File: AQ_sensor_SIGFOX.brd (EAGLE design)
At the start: 110 x 64 mm, 49 parts, among them IC2 MCP73831/OT, J1 F-1X03-SIP-100-32, SW1 PCM12SMTR, SW2 PCM12SMTR, U2 TEXAS_INSTRUMENTS_SN74HC125TE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, U3 TEXAS_INSTRUMENTS_LM1117IMP-3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, X1 53048-08, X2 SIMLOCK-C707_10M006_512_2, X4 50 Ohms

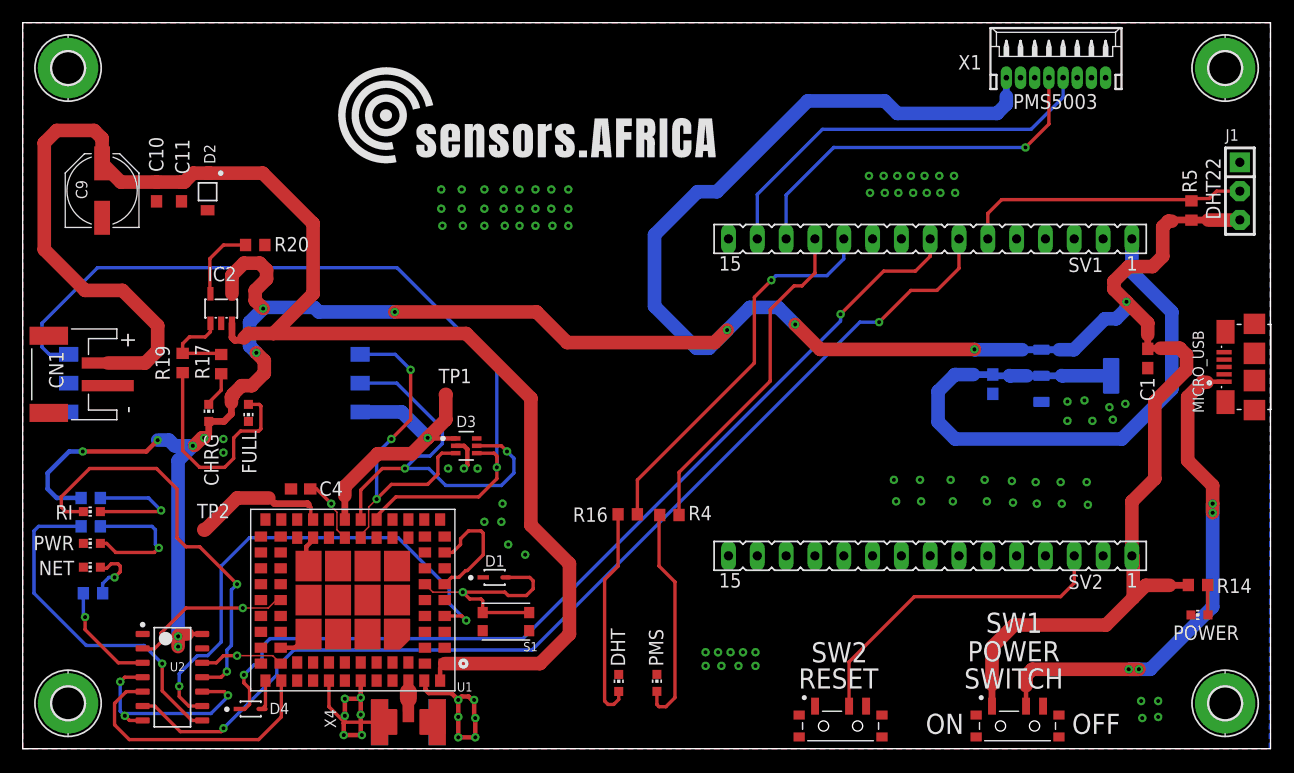
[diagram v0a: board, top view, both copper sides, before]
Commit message: Added sigfox circuit
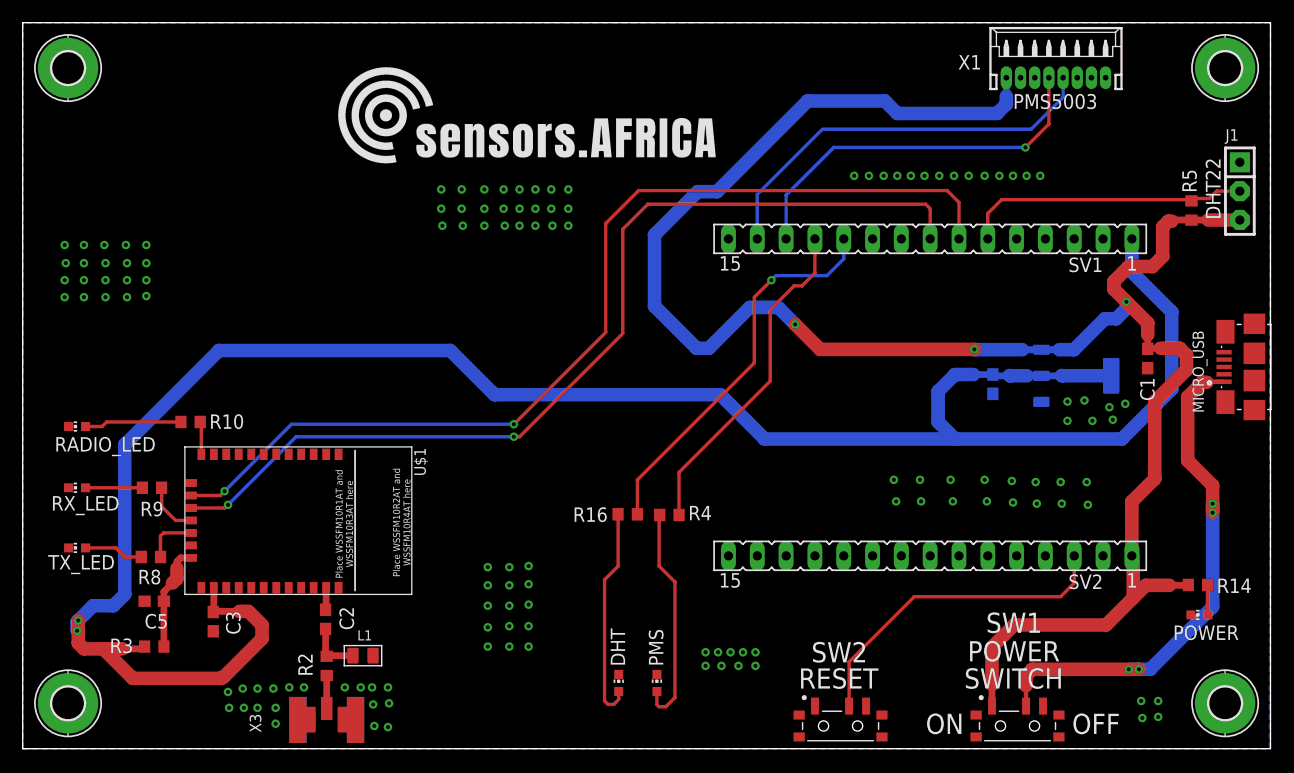
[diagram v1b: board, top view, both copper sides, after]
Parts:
- removed C10: 33pF, rcl:C0603
- removed C11: 10pF, rcl:C0603
- removed C4: 10uF, rcl:C0603
- removed C9: 100uF, rcl:PANASONIC_D
- removed CHRG, PWR: RED, led:CHIP-LED0603
- removed CN1: (no value), AQ_sensor_GSM:JST-PH-2-SMT-RA
- removed D1, D4: ON_SEMI_1N4148WSON_SEMI_1N4148WS_0_0, AQ_sensor_GSM:ON_SEMI_1N4148WS_0
- removed D2: ON_SEMICONDUCTOR_MMSZ5231BT1GON_SEMICONDUCTOR_MMSZ5231BT1G_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, AQ_sensor_GSM:ON_SEMICONDUCTOR_MMSZ5231BT1G_0
- removed D3: SEMTECH_SMF05CSEMTECH_SMF05C_0_0, AQ_sensor_GSM:SEMTECH_SMF05C_0
- removed FULL, NET: YELLOW, led:CHIP-LED0603
- removed IC2: MCP73831/OT, AQ_sensor_GSM:SOT23-5L
- removed R1, R17, R19, R6, R7: 470, rcl:R0603
- removed R20: 2K, rcl:R0603
- removed RI: ORANGE, led:CHIP-LED0603
- removed S1: KMR621NGLFS, AQ_sensor_GSM:SW_KMR621NGLFS
- removed TP1, TP2: TPB1,27, testpad:B1,27
- removed U1: (no value), AQ_sensor_GSM:SIM800L
- removed U2: TEXAS_INSTRUMENTS_SN74HC125TEXAS_INSTRUMENTS_SN74HC125_0_0, AQ_sensor_GSM:TEXAS_INSTRUMENTS_SN74HC125_0
- removed X2: SIMLOCK-C707_10M006_512_2, AQ_sensor_GSM:C707_10M006_512_2
- removed X4: 50 Ohms, AQ_sensor_GSM:SMA_EDGELAUNCH_UFL
- added C2: 100pF, rcl:C0603
- added C3, C5: 100nF, rcl:C0603
- added L1: 47NH, OPL_Inductor:L0805
- added R10, R8, R9: 470, rcl:R0603
- added R2: 0R, rcl:R0603
- added R3: 100K 1/16W, rcl:R0603
- added RADIO_LED: ORANGE, led:CHIP-LED0603
- added RX_LED, TX_LED: GREEN, led:CHIP-LED0603
- added U$1: WSSFM10RWSSFM10R2R4, WisolWSSFM10R:WSSFM10R
- added X3: (no value), AQ_sensor_GSM:SMA_EDGELAUNCH_UFL
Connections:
- removed net 1.8V: D3.1, TP1.TP, U1.16, X2.C1
- removed net 2.8V: TP2.TP, U1.18
- removed net GSM_ANT: U1.40, X4.P
- removed net GSM_RST: U1.49
- removed net GSM_RST_O: SV1.5
- removed net GSM_RX: D4.2, U1.31
- removed net GSM_RX_O: D4.1, SV1.8
- removed net GSM_TX: U1.32, U2.5
- removed net GSM_TX_5V: SV1.7, U2.6
- removed net N$10: NET.A, R6.2
- removed net N$11: PWR.A, R7.2
- removed net N$12: FULL.A, R19.1
- removed net N$13: IC2.5, R20.1
- removed net N$14: R1.2, RI.A
- removed net N$6: CHRG.C, R17.1
- removed net N$9: IC2.1, R17.2, R19.2
- removed net NETSTAT: U1.64, U2.2
- removed net NETSTAT_5V: R6.1, U2.3
- removed net PWRKEY: D1.2, S1.2_1, S1.2_2, U1.48
- removed net PWRSTAT: U1.4, U2.9
- removed net PWRSTAT_5V: R7.1, U2.8
- removed net RI: U1.68, U2.12
- removed net RI_5V: RI.C, U2.11
- removed net SIMCLK: D3.3, U1.55, X2.C3
- removed net SIMDATA: D3.4, U1.14, X2.C7
- removed net SIMRST: D3.5, U1.15, X2.C2
- removed net VBUS: U1.7
- removed net VRTC: C4.1, U1.56
- removed net V_LIPO: C10.1, C11.1, C9.+, CN1.1, D2.1, IC2.3, U1.1, U1.42
- new net N$1: C2.1, U$1.30
- new net N$15: R8.2, TX_LED.A
- new net N$2: C2.2, L1.1, R2.2
- new net N$3: R2.1, X3.P
- new net N$5: C5.1, R3.2, U$1.19
- new net N$7: R10.2, RADIO_LED.A
- new net N$8: R9.2, RX_LED.A
- new net RADIO_LED: R10.1, U$1.12
- new net RX_LED: R9.1, U$1.16
- new net TX_LED: R8.1, U$1.17
- new net WISOL_RX: SV1.8, U$1.15
- new net WISOL_TX: SV1.7, U$1.14
- new net WISON_RST: U$1.13
- net +3V3: now also C3.1, R3.1, U$1.21
- net +5V: no longer CHRG.A, IC2.4, R1.1, U2.14
- net GND: now also C3.2, C5.2, L1.2, RADIO_LED.C, RX_LED.C, TX_LED.C, U$1.1, U$1.2, U$1.20, U$1.28, U$1.29, U$1.3, U$1.31, U$1.4, X3.GND@1, X3.GND@2, X3.GND@3, X3.GND@4; no longer C10.2, C11.2, C4.2, C9.-, CN1.2, D1.1, D2.2, D3.2, FULL.C, IC2.2, NET.C, PWR.C, R20.2, S1.1_1, S1.1_2, U1.2, U1.35, U1.37, U1.38, U1.39, U1.41, U1.43, U1.44, U1.45, U1.58, U1.6, U1.67, U1.71, U1.72, U1.73, U1.76, U1.77, U1.78, U1.79, U1.8, U1.80, U1.81, U1.82, U1.83, U1.84, U1.85, U1.86, U1.87, U1.88, U2.1, U2.10, U2.13, U2.4, U2.7, X2.C5, X4.GND@1, X4.GND@2, X4.GND@3, X4.GND@4
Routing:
- net V_LIPO: track 136.5 -> 0.00 mm
- net +3V3: track 56.9 -> 188.9 mm, vias 0 -> 2
- net +5V: track 277.6 -> 168.5 mm, vias 13 -> 3
- net GSM_TX_5V: track 92.9 -> 0.00 mm, vias 2 -> 0
- net WISOL_TX: track 0.00 -> 88.1 mm, vias 0 -> 2
- net WISOL_RX: track 0.00 -> 84.4 mm, vias 0 -> 2
- net GSM_RX_O: track 82.4 -> 0.00 mm, vias 2 -> 0
- net SIMDATA: track 75.4 -> 0.00 mm, vias 1 -> 0
- net GND: track 71.6 -> 0.00 mm, vias 99 -> 128
- net PWRSTAT: track 44.4 -> 0.00 mm, vias 2 -> 0
- net SIMRST: track 37.4 -> 0.00 mm, vias 2 -> 0
- net RI_5V: track 36.7 -> 0.00 mm, vias 2 -> 0
- net SIMCLK: track 31.2 -> 0.00 mm, vias 3 -> 0
- net PWRSTAT_5V: track 30.7 -> 0.00 mm, vias 1 -> 0
- net 1.8V: track 25.9 -> 0.00 mm, vias 1 -> 0
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
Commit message: added via stitching
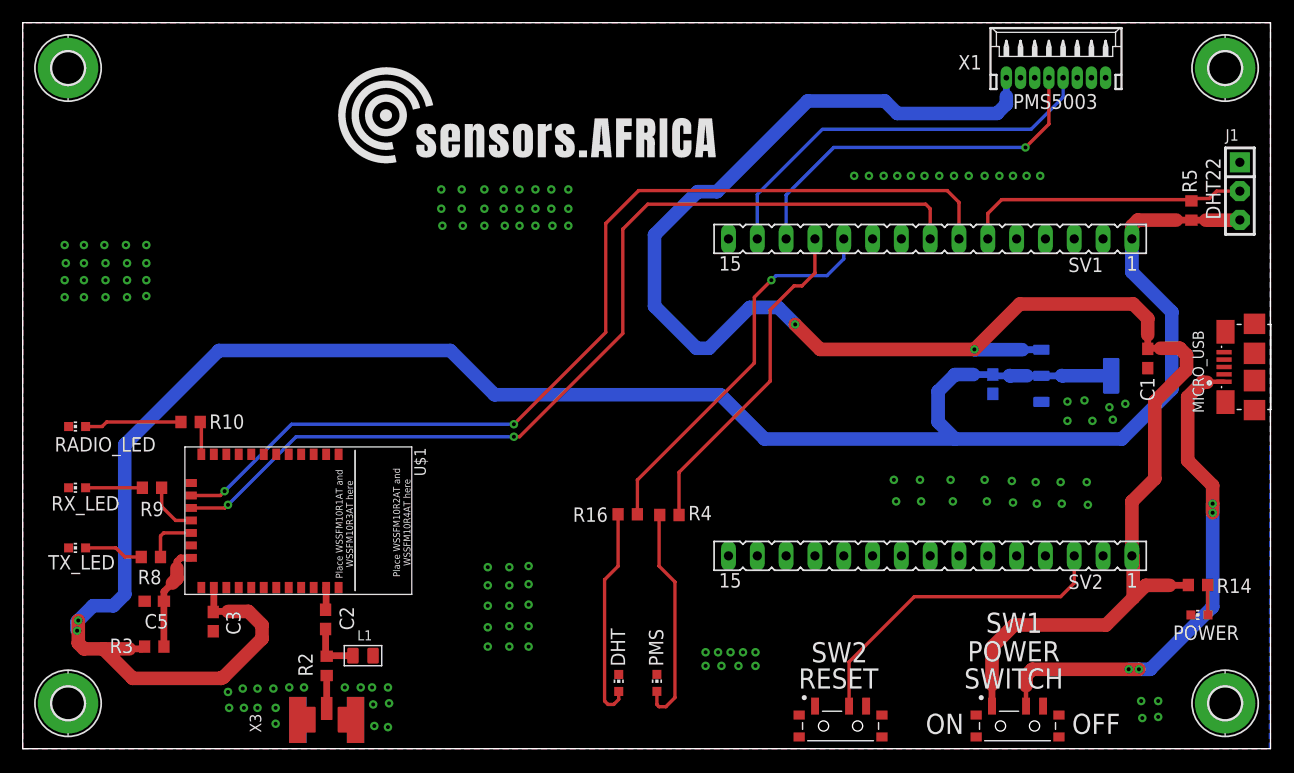
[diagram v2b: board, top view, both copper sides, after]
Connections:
- net +3V3: now also J1.3, R5.1
- net +5V: no longer J1.3, R5.1
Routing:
- net +5V: track 168.5 -> 156.6 mm, vias 3 -> 2
- net +3V3: track 188.9 -> 199.8 mm
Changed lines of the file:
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@@
 <drawing>
 <settings>
-<setting alwaysvectorfont="yes"/>
+<setting alwaysvectorfont="no"/>
 <setting verticaltext="up"/>
 </settings>
@@
 <contactref element="C1" pad="1"/>
 <contactref element="U3" pad="3"/>
-<contactref element="J1" pad="3"/>
-<contactref element="R5" pad="1"/>
 <contactref element="SW1" pad="1"/>
 <wire x1="102.51" y1="14.18" x2="102.76" y2="14.43" width="0.4" layer="1"/>
 <wire x1="89.775" y1="35.2" x2="89.805" y2="35.17" width="0.4" layer="16"/>
-<wire x1="103.05" y1="46.61" x2="103.03" y2="46.59" width="0.4" layer="1"/>
 <wire x1="85.45" y1="3.75" x2="85.45" y2="5.65" width="0.6" layer="1"/>
 <wire x1="85.5" y1="5.7" x2="85.45" y2="5.65" width="0.6" layer="1"/>
@@
 <wire x1="99.18" y1="35.25" x2="99.18" y2="36.48" width="0.6" layer="1"/>
 <wire x1="99.18" y1="36.48" x2="99.2" y2="36.5" width="0.6" layer="1"/>
-<wire x1="99.18" y1="36.48" x2="99.18" y2="37.52" width="1.2" layer="1"/>
-<wire x1="99.18" y1="37.52" x2="97.3" y2="39.4" width="1.2" layer="1"/>
-<via x="97.3" y="39.4" extent="1-16" drill="0.35"/>
-<wire x1="97.3" y1="39.4" x2="96.2" y2="40.5" width="1.2" layer="1"/>
-<wire x1="97.5" y1="42.5" x2="99.6" y2="42.5" width="1.2" layer="1"/>
-<wire x1="99.6" y1="42.5" x2="100.5" y2="43.4" width="1.2" layer="1"/>
-<wire x1="96.2" y1="40.5" x2="96.2" y2="41.2" width="1.2" layer="1"/>
-<wire x1="96.2" y1="41.2" x2="97.5" y2="42.5" width="1.2" layer="1"/>
-<wire x1="101.3" y1="46.5" x2="101" y2="46.5" width="1.2" layer="1"/>
-<wire x1="100.5" y1="43.4" x2="100.5" y2="46" width="1.2" layer="1"/>
-<wire x1="100.5" y1="46" x2="101" y2="46.5" width="1.2" layer="1"/>
-<wire x1="101" y1="46.5" x2="101.11" y2="46.61" width="0.6" layer="1"/>
-<wire x1="101.11" y1="46.61" x2="103.05" y2="46.61" width="0.6" layer="1"/>
-<wire x1="103.03" y1="46.59" x2="103.04" y2="46.6" width="0.6" layer="1"/>
-<wire x1="103.04" y1="46.6" x2="104.5" y2="46.6" width="0.6" layer="1"/>
-<wire x1="104.5" y1="46.6" x2="107.29" y2="46.6" width="1.2" layer="1"/>
-<wire x1="107.29" y1="46.6" x2="107.3" y2="46.61" width="1.2" layer="1"/>
-<wire x1="89.805" y1="35.17" x2="91.37" y2="35.17" width="0.6" layer="16"/>
-<wire x1="91.37" y1="35.17" x2="91.4" y2="35.2" width="0.6" layer="16"/>
-<wire x1="91.37" y1="35.17" x2="92.67" y2="35.17" width="1.2" layer="16"/>
-<wire x1="95.4" y1="37.9" x2="96.4" y2="37.9" width="1.2" layer="16"/>
-<wire x1="96.4" y1="37.9" x2="97.3" y2="38.8" width="1.2" layer="16"/>
-<wire x1="97.3" y1="38.8" x2="97.3" y2="39.4" width="1.2" layer="16"/>
-<wire x1="92.67" y1="35.17" x2="95.4" y2="37.9" width="1.2" layer="16"/>
 <wire x1="89.805" y1="35.17" x2="88.13" y2="35.17" width="0.6" layer="16"/>
 <wire x1="88.13" y1="35.17" x2="88.1" y2="35.2" width="0.6" layer="16"/>
@@
 <wire x1="85.9" y1="56" x2="86.715" y2="56.815" width="1.2" layer="16"/>
 <wire x1="60.5" y1="35.3" x2="64.1" y2="38.9" width="1.2" layer="16"/>
+<wire x1="99.18" y1="36.48" x2="99.18" y2="37.92" width="1.2" layer="1"/>
+<wire x1="99.18" y1="37.92" x2="97.9" y2="39.2" width="1.2" layer="1"/>
+<wire x1="87.9" y1="39.2" x2="83.9" y2="35.2" width="1.2" layer="1"/>
+<wire x1="97.9" y1="39.2" x2="87.9" y2="39.2" width="1.2" layer="1"/>
 </signal>
 <signal name="+3V3" class="1">
@@
 <wire x1="4.9" y1="9.3" x2="5.4" y2="8.8" width="1.2" layer="1"/>
 <wire x1="5.4" y1="8.8" x2="7.1" y2="8.8" width="1.2" layer="1"/>
-<wire x1="7.1" y1="8.8" x2="8.8" y2="8.8" width="1.2" layer="1"/>
-<wire x1="8.8" y1="8.8" x2="10.55" y2="8.8" width="0.6" layer="1"/>
 <wire x1="10.55" y1="8.8" x2="10.75" y2="9" width="0.6" layer="1"/>
 <wire x1="7.1" y1="8.8" x2="9.7" y2="6.2" width="1.2" layer="1"/>
@@
 <wire x1="21.1" y1="9.7" x2="21.1" y2="10.9" width="1.2" layer="1"/>
 <wire x1="21.1" y1="10.9" x2="19.9" y2="12.1" width="1.2" layer="1"/>
-<wire x1="19.9" y1="12.1" x2="19.1" y2="12.1" width="1.2" layer="1"/>
 <wire x1="9.7" y1="6.2" x2="17.49235" y2="6.2" width="1.2" layer="1"/>
 <wire x1="17.6782" y1="6.2782" x2="21.1" y2="9.7" width="1.2" layer="1"/>
-<wire x1="19.1" y1="12.1" x2="16.85" y2="12.1" width="0.6" layer="1"/>
+<contactref element="R5" pad="1"/>
+<wire x1="103.03" y1="46.59" x2="103.04" y2="46.6" width="0.6" layer="1"/>
+<contactref element="J1" pad="3"/>
+<wire x1="97.78" y1="44.94" x2="97.78" y2="46.08" width="1.2" layer="1"/>
+<wire x1="98.3" y1="46.6" x2="101.7" y2="46.6" width="1.2" layer="1"/>
+<wire x1="97.78" y1="46.08" x2="98.3" y2="46.6" width="1.2" layer="1"/>
+<wire x1="101.7" y1="46.6" x2="103.02" y2="46.6" width="0.6" layer="1"/>
+<wire x1="103.02" y1="46.6" x2="103.03" y2="46.59" width="0.6" layer="1"/>
+<wire x1="103.03" y1="46.59" x2="104.29" y2="46.59" width="0.6" layer="1"/>
+<wire x1="104.29" y1="46.59" x2="104.3" y2="46.6" width="0.6" layer="1"/>
+<wire x1="104.29" y1="46.59" x2="107.28" y2="46.59" width="1.2" layer="1"/>
+<wire x1="107.28" y1="46.59" x2="107.3" y2="46.61" width="1.2" layer="1"/>
+<wire x1="19.9" y1="12.1" x2="18.1" y2="12.1" width="1.2" layer="1"/>
+<wire x1="18.1" y1="12.1" x2="16.85" y2="12.1" width="0.6" layer="1"/>
+<wire x1="7.1" y1="8.8" x2="9.4" y2="8.8" width="1.2" layer="1"/>
+<wire x1="9.4" y1="8.8" x2="10.55" y2="8.8" width="0.6" layer="1"/>
 </signal>
 <signal name="DHT_OUT">
